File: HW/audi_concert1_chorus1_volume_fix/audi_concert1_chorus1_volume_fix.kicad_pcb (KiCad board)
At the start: 2 copper layers, 34 x 26.2 mm, 42 parts, among them CON1 I2C_to_TDA, CON2 USB, CON3 SPI_TO_PANEL, CON4 JLINK, U1 68HC05_PLCC, U2 AP1117-33, U3 STM32F103C8Tx, U4 MAX809, Y1 32.768kHz, Y2 8MHz

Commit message: v4
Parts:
- moved R17 0.23 mm to (128.0, 95.6)
- moved D1 0.10 mm to (121.9, 93.2)
- moved R15 0.07 mm to (124.2, 93.7)
- moved R3 0.05 mm to (117.6, 93.2)
- moved R2 0.05 mm to (119.6, 93.2)
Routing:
- net 3V3: track 120.5 -> 112.5 mm
- net /CLOCK_TO_PANEL: track 10.5 -> 11.6 mm
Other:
- board size 34 x 26.2 mm -> 35.1 x 27.2 mm

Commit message: HW v4
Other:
- rule pad_to_mask_clearance: 0.2 -> 0.05
- rule solder_mask_min_width: 0.25 -> 0.05
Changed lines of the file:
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@@
     (pad_size 1.524 1.524)
     (pad_drill 0.762)
-    (pad_to_mask_clearance 0.2)
-    (solder_mask_min_width 0.25)
+    (pad_to_mask_clearance 0.05)
+    (solder_mask_min_width 0.05)
     (aux_axis_origin 0 0)
     (visible_elements FFFFFF7F)

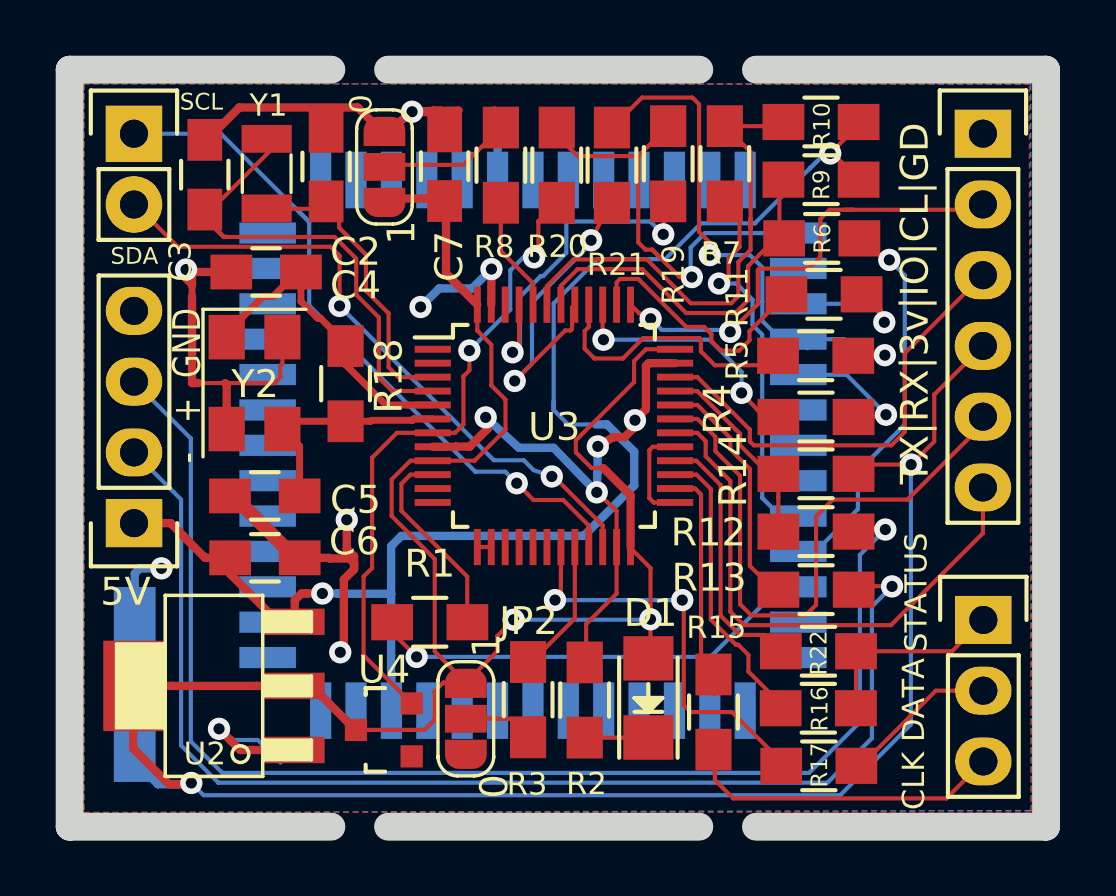
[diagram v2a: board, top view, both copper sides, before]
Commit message: vias changed to 0.5/0.3
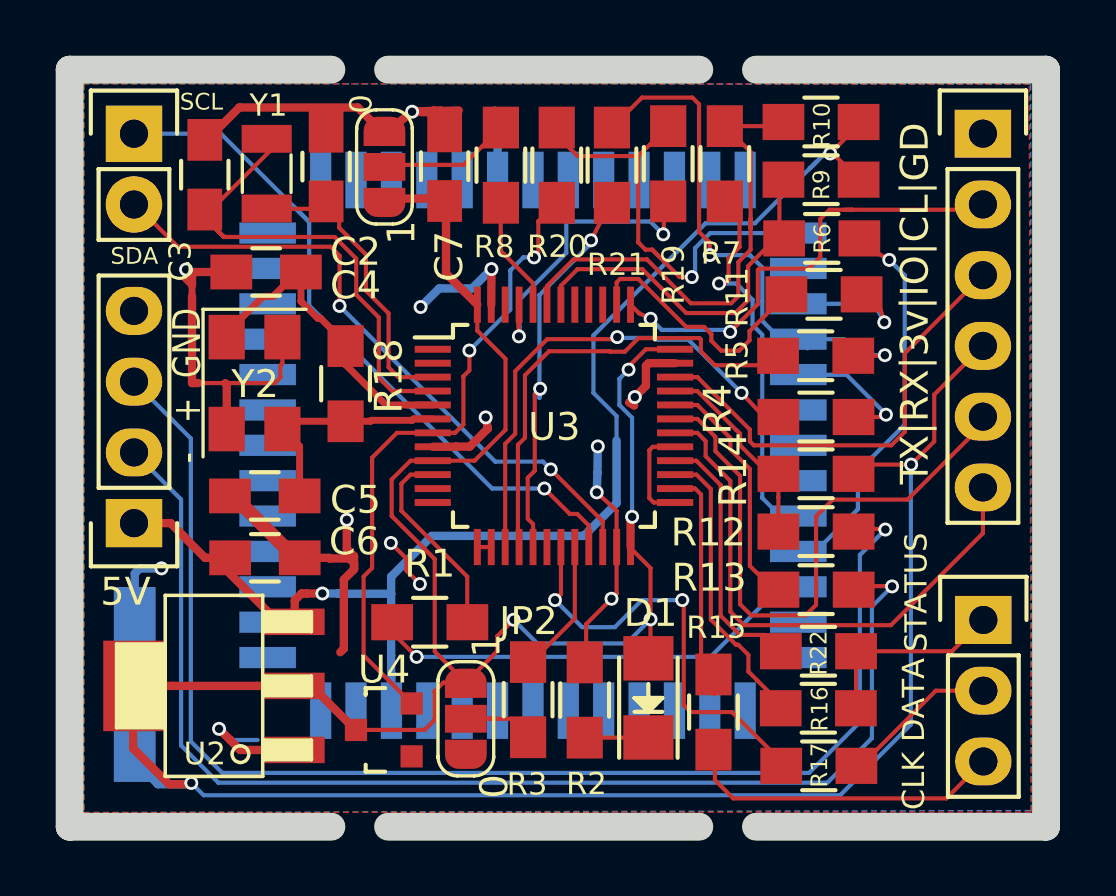
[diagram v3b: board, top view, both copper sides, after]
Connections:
- U3 pad 15: (no net) -> Net-(R4-Pad1)
- U3 pad 16: (no net) -> Net-(R5-Pad2)
- U3 pad 17: (no net) -> Net-(R21-Pad2)
- U3 pad 39: Net-(R4-Pad1) -> (no net)
- U3 pad 40: Net-(R5-Pad2) -> (no net)
- U3 pad 41: Net-(R21-Pad2) -> (no net)
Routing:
- net Net-(R4-Pad1): track 9.15 -> 17.6 mm
- net Net-(R5-Pad2): track 9.82 -> 16.7 mm
- net GND: track 73.9 -> 67.6 mm, vias 12 -> 14
- net 5V: track 52.3 -> 47.4 mm
- net Net-(R21-Pad2): track 11.5 -> 14.3 mm
- net Net-(R19-Pad2): track 13.0 -> 11.6 mm
- net Net-(R17-Pad2): track 14.8 -> 15.6 mm
- net 3V3: track 112.5 -> 111.8 mm, vias 4 -> 6
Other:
- net class 3v3: via_dia 0.8 -> 0.5; via_drill 0.4 -> 0.3
- net class 5V: via_dia 0.8 -> 0.5; via_drill 0.4 -> 0.3
- net class Default: via_dia 0.8 -> 0.5; via_drill 0.4 -> 0.3
- net class GND: via_dia 0.8 -> 0.5; via_drill 0.4 -> 0.3
- board text added: "v5.0"
- board text removed: "AUDI"
- board text removed: "v4.0"

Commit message: gala input fix 11+10 togeter
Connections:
- U3 pad 11: (no net) -> Net-(R1-Pad2)
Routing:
- net GND: track 67.6 -> 65.4 mm
- net Net-(R1-Pad2): track 7.28 -> 7.78 mm
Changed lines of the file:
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@@
     (thickness 1.6)
     (drawings 24)
-    (tracks 649)
+    (tracks 648)
     (modules 42)
     (nets 48)
@@
       (net 22 "Net-(R1-Pad2)") (pinfunction "ADC1_IN0/ADC2_IN0/SYS_WKUP/TIM2_CH1/TIM2_ETR/USART2_CTS/PA0"))
     (pad "11" smd rect (at -4.35 2.25) (size 1.3 0.25) (layers "F.Cu" "F.Paste" "F.Mask")
-      (pinfunction "ADC1_IN1/ADC2_IN1/TIM2_CH2/USART2_RTS/PA1"))
+      (net 22 "Net-(R1-Pad2)") (pinfunction "ADC1_IN1/ADC2_IN1/TIM2_CH2/USART2_RTS/PA1"))
     (pad "12" smd rect (at -4.35 2.75) (size 1.3 0.25) (layers "F.Cu" "F.Paste" "F.Mask")
       (pinfunction "ADC1_IN2/ADC2_IN2/TIM2_CH3/USART2_TX/PA2"))
@@
     (effects (font (size 1 1) (thickness 0.15)) (justify mirror))
   )
+  (segment (start 114.1283 85.6509) (end 114.1283 85.1509) (width 0.15) (layer "F.Cu") (net 22))
+  (segment (start 113.3856 72.1233) (end 113.8482 72.1233) (width 0.5) (layer "F.Cu") (net 1))
+  (segment (start 113.8482 72.1233) (end 114.554 72.8291) (width 0.5) (layer "F.Cu") (net 1))
   (segment (start 113.665 89.0778) (end 113.1824 88.5952) (width 0.15) (layer "F.Cu") (net 1))
   (segment (start 113.1824 88.5952) (end 113.1824 88.1634) (width 0.15) (layer "F.Cu") (net 1))
@@
   (segment (start 115.23346 74.03084) (end 116.5733 72.691) (width 0.15) (layer "F.Cu") (net 20))
   (segment (start 115.09756 74.03084) (end 115.23346 74.03084) (width 0.15) (layer "F.Cu") (net 20))
-  (segment (start 113.3856 72.1233) (end 114.4143 72.07758) (width 0.3) (layer "F.Cu") (net 1))
-  (segment (start 113.3856 72.1233) (end 114.23238 72.1522) (width 0.3) (layer "F.Cu") (net 1))
   (via (at 113.3856 72.1233) (size 0.5) (drill 0.3) (layers "F.Cu" "B.Cu") (net 1))
-  (segment (start 113.3856 72.1233) (end 115.06232 72.07758) (width 0.3) (layer "F.Cu") (net 1))
   (segment (start 114.33 75.2394) (end 114.6048 75.5142) (width 0.3) (layer "F.Cu") (net 7))
   (segment (start 114.6048 75.5142) (end 114.6048 77.9274) (width 0.3) (layer "F.Cu") (net 7))
@@
   (segment (start 116.454601 72.192561) (end 116.454601 74.5744) (width 0.3) (layer "B.Cu") (net 1))
   (segment (start 114.33968 72.1522) (end 114.23238 72.1522) (width 0.3) (layer "F.Cu") (net 1))
-  (segment (start 114.23238 72.1522) (end 114.15776 72.07758) (width 0.3) (layer "F.Cu") (net 1))
   (segment (start 123.760149 89.028351) (end 123.760149 92.552449) (width 0.15) (layer "F.Cu") (net 37))
   (segment (start 123.760149 92.552449) (end 124.2441 93.0364) (width 0.15) (layer "F.Cu") (net 37))

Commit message: HW v5
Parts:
- added R23: 1k, Resistors_SMD.pretty:R_0805_HandSoldering, F.Cu at (114.2, 90.4)
- added R24: 100, Resistors_SMD.pretty:R_0805_HandSoldering, F.Cu at (111.5, 86.8)
- R19: value 1k -> NP
- moved R1 6.04 mm to (120.1, 90.4), turned to 180 degrees
- moved R3 1.47 mm to (117.8, 94.7)
- moved R2 1.47 mm to (119.9, 94.7)
- moved D1 1.01 mm to (122.2, 94.1)
- moved JP2 0.83 mm to (115.3, 94.7)
- moved R15 0.64 mm to (124.5, 94.2)
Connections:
- U3 pad 10: Net-(R1-Pad2) -> Net-(R23-Pad2)
- U3 pad 11: Net-(R1-Pad2) -> (no net)
- U3 pad 40: (no net) -> Net-(R1-Pad2)
- U3 pad 41: (no net) -> Net-(R1-Pad2)
- U4 pad 2: /RESET -> Net-(R24-Pad2)
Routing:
- net /RESET_KA: track 15.9 -> 33.2 mm, vias 1 -> 3
- net /GALA: track 16.4 -> 6.96 mm
- net Net-(R1-Pad2): track 7.78 -> 16.6 mm
- net /RESET: track 23.0 -> 14.4 mm
- net Net-(R23-Pad2): track 0.00 -> 6.29 mm
- net Net-(R24-Pad2): track 0.00 -> 6.09 mm
- net GND: track 65.4 -> 61.8 mm, vias 14 -> 13
- net 3V3: track 111.8 -> 114.2 mm, vias 6 -> 4
- net Net-(R3-Pad1): track 5.33 -> 7.52 mm
- net Net-(R5-Pad2): track 16.7 -> 15.8 mm
- net /BOOT1: track 3.67 -> 2.74 mm
- net Net-(R4-Pad1): track 17.6 -> 16.8 mm
- net Net-(R19-Pad2): track 11.6 -> 11.0 mm
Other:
- board size 35.1 x 27.2 mm -> 34.2 x 26.3 mm

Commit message: HWv5 fix
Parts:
- moved CON3 1.56 mm to (132.3, 90.4)
- moved CON4 1.54 mm to (132.3, 72.9)
- turned C8 to -90 degrees
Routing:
- net /STATUS_FROM_MCU: track 6.19 -> 3.07 mm
- net GND: track 61.8 -> 64.5 mm, vias 13 -> 15
- net Net-(CON2-Pad3): track 47.5 -> 45.2 mm
- net /CLOCK_FROM_MCU: track 4.93 -> 2.99 mm
- net /CLOCK_TO_PANEL: track 11.6 -> 9.79 mm
- net /DATA_TO_PANEL: track 8.28 -> 6.47 mm
- net /DATA_FROM_MCU: track 20.8 -> 19.0 mm
- net /SWDCLK: track 16.7 -> 15.1 mm
- net /SCL_FROM_MOTO: track 14.1 -> 13.0 mm
- net /STATUS_TO_PANEL: track 5.64 -> 4.83 mm
- net 3V3: track 114.2 -> 115.0 mm, vias 4 -> 5
- net Net-(CON2-Pad2): track 44.5 -> 43.8 mm
- net /TX: track 20.1 -> 19.5 mm
- net /RX: track 22.0 -> 21.8 mm, vias 0 -> 1
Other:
- board size 34.2 x 26.3 mm -> 33 x 27.2 mm
- board text removed: "CLK DATA"
- board text removed: "CL|DA|ST"
- board text removed: "STATUS"
- board text removed: "TX|RX|3v|IO|CL|GD"

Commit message: kicad6
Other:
- net class 3v3 removed
- net class 5V removed
- net class Default removed
- net class GND removed

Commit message: hwv5
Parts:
- C2, C3: value 22p -> 12p(NP)
- R12, R13: value 20 -> 20(NP)
- R14: value 1k5 -> 1k5(NP)
- R15, R16, R17: value 1k -> 1k(NP)
- R19: value NP -> 1k(NP)
- R22: value 10k -> 10k(NP)
- R24: value 100 -> 1k(NP)
- U4: value MAX809 -> MAX809(NP)
- Y1: value 32.768kHz -> 32.768kHz(NP)
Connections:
- U1 pad 1: (no net) -> unconnected-(U1-Pad1)
- U1 pad 11: (no net) -> unconnected-(U1-Pad11)
- U1 pad 12: (no net) -> unconnected-(U1-Pad12)
- U1 pad 13: (no net) -> unconnected-(U1-Pad13)
- U1 pad 14: (no net) -> unconnected-(U1-Pad14)
- U1 pad 15: (no net) -> unconnected-(U1-Pad15)
- U1 pad 16: (no net) -> unconnected-(U1-Pad16)
- U1 pad 17: (no net) -> unconnected-(U1-Pad17)
- U1 pad 18: (no net) -> /RESET_MOTO
- U1 pad 19: (no net) -> unconnected-(U1-Pad19)
- U1 pad 2: (no net) -> unconnected-(U1-Pad2)
- U1 pad 20: (no net) -> unconnected-(U1-Pad20)
- U1 pad 21: (no net) -> unconnected-(U1-Pad21)
- U1 pad 22: (no net) -> unconnected-(U1-Pad22)
- U1 pad 26: (no net) -> unconnected-(U1-Pad26)
- U1 pad 27: (no net) -> unconnected-(U1-Pad27)
- U1 pad 28: (no net) -> unconnected-(U1-Pad28)
- U1 pad 3: (no net) -> unconnected-(U1-Pad3)
- U1 pad 32: (no net) -> unconnected-(U1-Pad32)
- U1 pad 34: (no net) -> unconnected-(U1-Pad34)
- U1 pad 35: (no net) -> unconnected-(U1-Pad35)
- U1 pad 36: (no net) -> unconnected-(U1-Pad36)
- U1 pad 37: (no net) -> unconnected-(U1-Pad37)
- U1 pad 38: (no net) -> unconnected-(U1-Pad38)
- U1 pad 39: (no net) -> unconnected-(U1-Pad39)
- U1 pad 4: (no net) -> unconnected-(U1-Pad4)
- U1 pad 40: (no net) -> unconnected-(U1-Pad40)
- U1 pad 42: (no net) -> unconnected-(U1-Pad42)
- U1 pad 43: (no net) -> unconnected-(U1-Pad43)
- U1 pad 44: (no net) -> unconnected-(U1-Pad44)
- U1 pad 45: (no net) -> unconnected-(U1-Pad45)
- U1 pad 46: (no net) -> unconnected-(U1-Pad46)
- U1 pad 47: (no net) -> unconnected-(U1-Pad47)
- U1 pad 48: (no net) -> unconnected-(U1-Pad48)
- U1 pad 49: (no net) -> unconnected-(U1-Pad49)
- U1 pad 5: (no net) -> unconnected-(U1-Pad5)
- U1 pad 50: (no net) -> unconnected-(U1-Pad50)
- U1 pad 51: (no net) -> unconnected-(U1-Pad51)
- U1 pad 52: (no net) -> unconnected-(U1-Pad52)
- U1 pad 6: (no net) -> unconnected-(U1-Pad6)
- U1 pad 7: (no net) -> unconnected-(U1-Pad7)
- U1 pad 8: (no net) -> unconnected-(U1-Pad8)
- U1 pad 9: (no net) -> unconnected-(U1-Pad9)
- U3 pad 1: (no net) -> +BATT
- U3 pad 11: (no net) -> unconnected-(U3-Pad11)
- U3 pad 12: (no net) -> unconnected-(U3-Pad12)
- U3 pad 18: (no net) -> unconnected-(U3-Pad18)
- U3 pad 2: (no net) -> unconnected-(U3-Pad2)
- U3 pad 39: (no net) -> unconnected-(U3-Pad39)
- U3 pad 46: (no net) -> unconnected-(U3-Pad46)
